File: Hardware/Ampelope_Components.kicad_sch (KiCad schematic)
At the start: 101 parts, among them J18 SWD_Header, J19 USB_B_Micro, Q1 MMBT3904, Q2 MMBT3904, Q3 MMBT3904, Q4 MMBT3904, U1 STM32G431RB, U2 AS3364, U3 LM1117-3.3, U4 TL074, U5 TL074, U6 TL074, Y1 8MHz 20pF

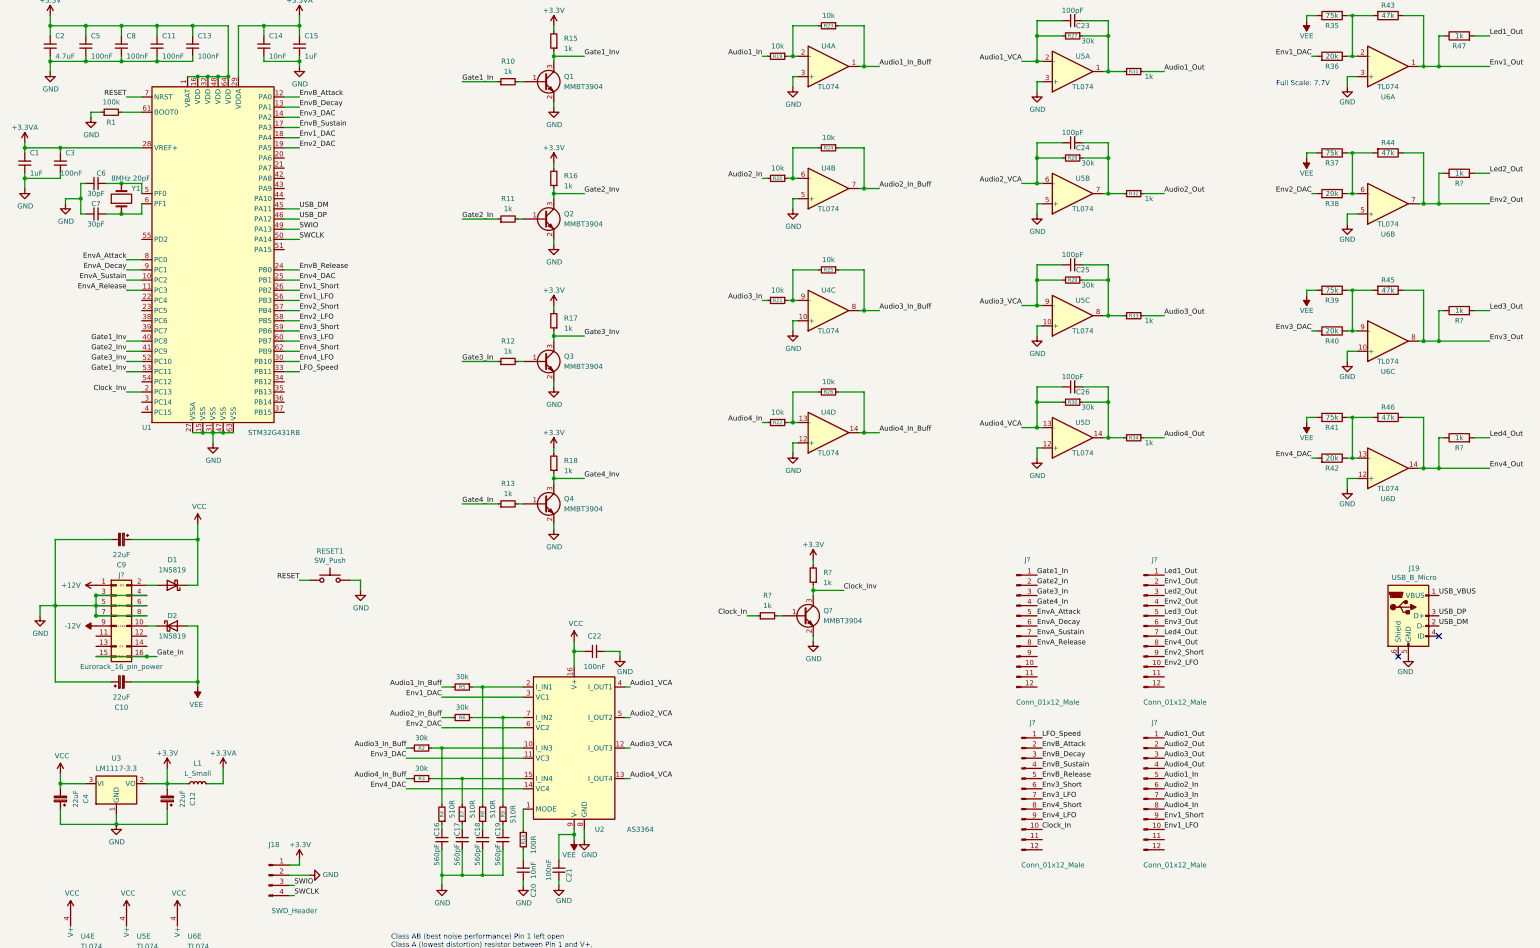
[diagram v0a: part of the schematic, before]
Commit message: Started rough placement of component board
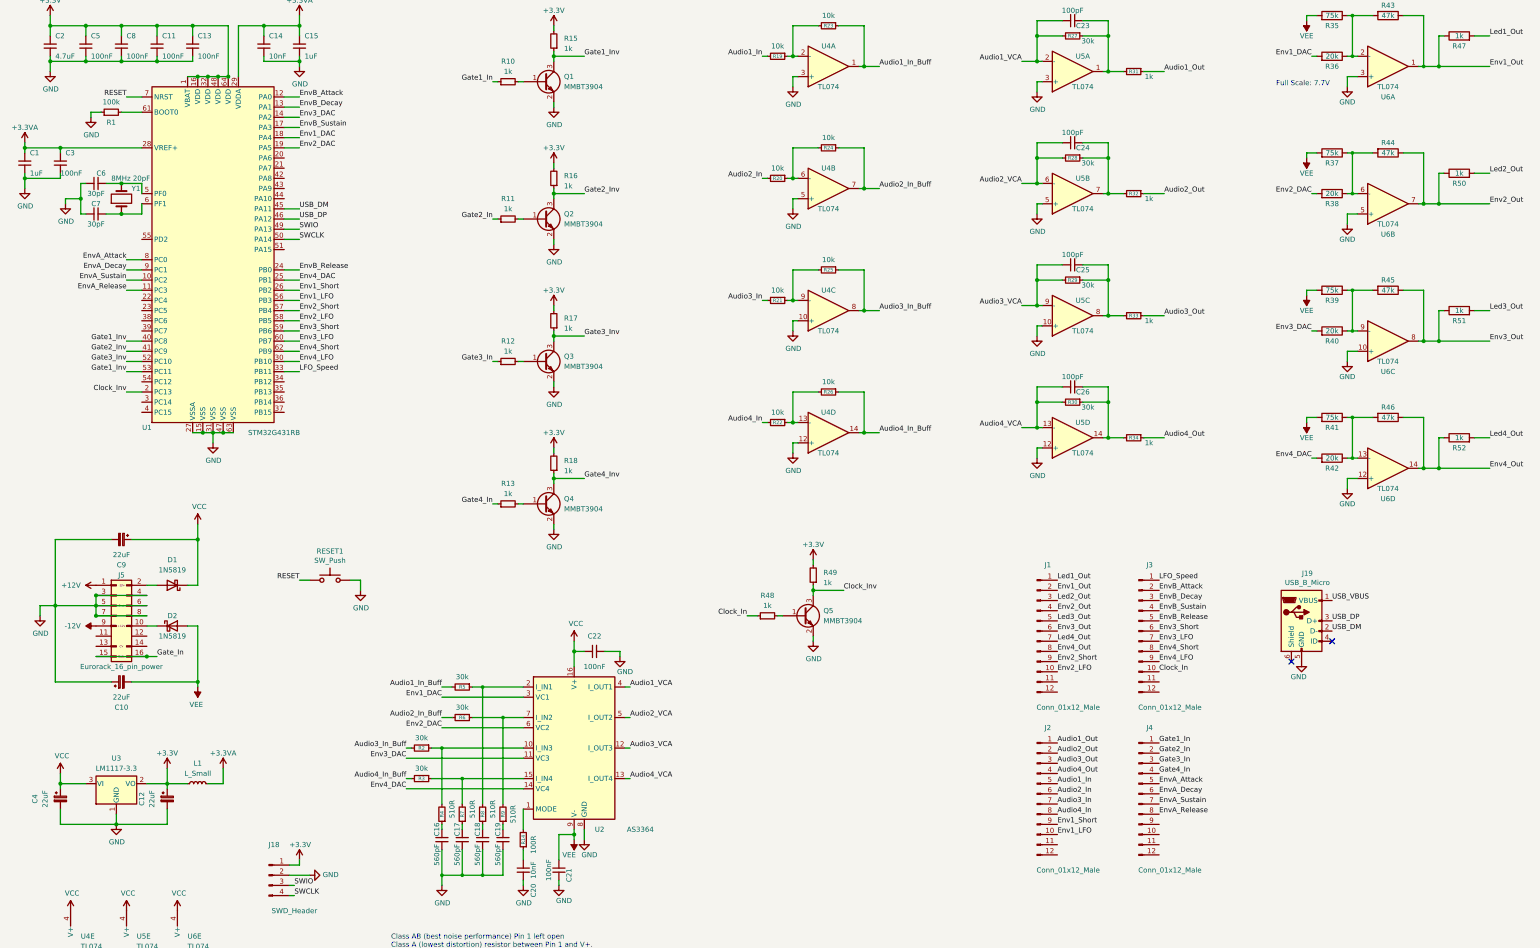
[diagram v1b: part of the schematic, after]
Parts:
- J1, J2, J3, J4: renamed from J?; footprint (none) -> Connector_PinHeader_2.54mm:PinHeader_1x12_P2.54mm_Vertical
- J5: renamed from J?; footprint (none) -> Custom_Footprints:Eurorack_16_pin_header
- gave numbers to parts that had none: 6
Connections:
- net +3V3: now also C12.1; no longer C12.2
- net GND: now also C12.2, C4.2; no longer C12.1, C4.1
- net VCC: now also C4.1; no longer C4.2
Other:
- moved on the sheet: C12, C4, J1, J19, J2, J3, J4

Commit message: More layout of component board
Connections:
- net +12V: now also D1.2 (A), J5.2 (Pin_2)
- net -12V: now also D2.1 (K), J5.10 (Pin_10)
- net Env1_Short: now also U1.42 (PA8); no longer U1.26 (PB2)
- net Env4_LFO: now also U1.43 (PA9); no longer U1.30 (PB10)
- net BOOT0: now reaches R1.2, U1.61 (BOOT0)
- no-connect marks 2 -> 6
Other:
- moved on the sheet: R1
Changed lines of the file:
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@@
   (junction (at 35.56 29.21) (diameter 1.016) (color 0 0 0 0))
   (junction (at 35.56 38.1) (diameter 1.016) (color 0 0 0 0))
+  (junction (at 38.1 168.91) (diameter 1.016) (color 0 0 0 0))
   (junction (at 38.1 171.45) (diameter 1.016) (color 0 0 0 0))
   (junction (at 38.1 173.99) (diameter 1.016) (color 0 0 0 0))
   (junction (at 38.1 176.53) (diameter 1.016) (color 0 0 0 0))
+  (junction (at 38.1 179.07) (diameter 1.016) (color 0 0 0 0))
   (junction (at 43.18 228.6) (diameter 1.016) (color 0 0 0 0))
   (junction (at 44.45 29.21) (diameter 1.016) (color 0 0 0 0))
@@
   (junction (at 44.45 68.58) (diameter 1.016) (color 0 0 0 0))
   (junction (at 44.45 76.2) (diameter 1.016) (color 0 0 0 0))
+  (junction (at 50.8 168.91) (diameter 1.016) (color 0 0 0 0))
+  (junction (at 50.8 179.07) (diameter 1.016) (color 0 0 0 0))
   (junction (at 50.8 186.69) (diameter 1.016) (color 0 0 0 0))
   (junction (at 53.34 29.21) (diameter 1.016) (color 0 0 0 0))
@@
   (junction (at 373.38 107.95) (diameter 1.016) (color 0 0 0 0))
   (junction (at 373.38 139.7) (diameter 1.016) (color 0 0 0 0))
+  (no_connect (at 38.1 181.61))
+  (no_connect (at 38.1 184.15))
+  (no_connect (at 50.8 181.61))
+  (no_connect (at 50.8 184.15))
   (no_connect (at 336.55 187.96))
   (no_connect (at 346.71 182.88))
@@
     (stroke (width 0) (type solid) (color 0 0 0 0))
   )
+  (wire (pts (xy 30.48 50.8) (xy 33.02 50.8))
+    (stroke (width 0) (type solid) (color 0 0 0 0))
+  )
+  (wire (pts (xy 30.48 52.07) (xy 30.48 50.8))
+    (stroke (width 0) (type solid) (color 0 0 0 0))
+  )
   (wire (pts (xy 30.48 72.39) (xy 34.29 72.39))
     (stroke (width 0) (type solid) (color 0 0 0 0))
@@
     (stroke (width 0) (type solid) (color 0 0 0 0))
   )
-  (wire (pts (xy 36.83 50.8) (xy 39.37 50.8))
-    (stroke (width 0) (type solid) (color 0 0 0 0))
-  )
-  (wire (pts (xy 36.83 52.07) (xy 36.83 50.8))
+  (wire (pts (xy 38.1 50.8) (xy 49.53 50.8))
+    (stroke (width 0) (type solid) (color 0 0 0 0))
+  )
+  (wire (pts (xy 38.1 168.91) (xy 50.8 168.91))
     (stroke (width 0) (type solid) (color 0 0 0 0))
   )
@@
     (stroke (width 0) (type solid) (color 0 0 0 0))
   )
+  (wire (pts (xy 38.1 179.07) (xy 50.8 179.07))
+    (stroke (width 0) (type solid) (color 0 0 0 0))
+  )
   (wire (pts (xy 38.1 186.69) (xy 50.8 186.69))
     (stroke (width 0) (type solid) (color 0 0 0 0))
@@
     (stroke (width 0) (type solid) (color 0 0 0 0))
   )
-  (wire (pts (xy 44.45 50.8) (xy 49.53 50.8))
-    (stroke (width 0) (type solid) (color 0 0 0 0))
-  )
   (wire (pts (xy 44.45 68.58) (xy 49.53 68.58))
     (stroke (width 0) (type solid) (color 0 0 0 0))
@@
     (stroke (width 0) (type solid) (color 0 0 0 0))
   )
+  (wire (pts (xy 85.09 67.31) (xy 88.9 67.31))
+    (stroke (width 0) (type solid) (color 0 0 0 0))
+  )
+  (wire (pts (xy 85.09 69.85) (xy 88.9 69.85))
+    (stroke (width 0) (type solid) (color 0 0 0 0))
+  )
   (wire (pts (xy 85.09 74.93) (xy 88.9 74.93))
     (stroke (width 0) (type solid) (color 0 0 0 0))
@@
     (stroke (width 0) (type solid) (color 0 0 0 0))
   )
-  (wire (pts (xy 85.09 95.25) (xy 88.9 95.25))
-    (stroke (width 0) (type solid) (color 0 0 0 0))
-  )
   (wire (pts (xy 85.09 97.79) (xy 88.9 97.79))
     (stroke (width 0) (type solid) (color 0 0 0 0))
@@
   )
   (wire (pts (xy 85.09 110.49) (xy 88.9 110.49))
-    (stroke (width 0) (type solid) (color 0 0 0 0))
-  )
-  (wire (pts (xy 85.09 113.03) (xy 88.9 113.03))
     (stroke (width 0) (type solid) (color 0 0 0 0))
   )
@@
     (effects (font (size 1.27 1.27)) (justify left bottom))
   )
+  (label "BOOT0" (at 39.37 50.8 0)
+    (effects (font (size 1.27 1.27)) (justify left bottom))
+  )
   (label "RESET" (at 45.72 46.99 180)
     (effects (font (size 1.27 1.27)) (justify right bottom))
@@
     (effects (font (size 1.27 1.27)) (justify left bottom))
   )
+  (label "Env1_Short" (at 88.9 67.31 0)
+    (effects (font (size 1.27 1.27)) (justify left bottom))
+  )
+  (label "Env4_LFO" (at 88.9 69.85 0)
+    (effects (font (size 1.27 1.27)) (justify left bottom))
+  )
   (label "USB_DM" (at 88.9 74.93 0)
     (effects (font (size 1.27 1.27)) (justify left bottom))
@@
     (effects (font (size 1.27 1.27)) (justify left bottom))
   )
-  (label "Env1_Short" (at 88.9 95.25 0)
-    (effects (font (size 1.27 1.27)) (justify left bottom))
-  )
   (label "Env1_LFO" (at 88.9 97.79 0)
     (effects (font (size 1.27 1.27)) (justify left bottom))
@@
   )
   (label "Env4_Short" (at 88.9 110.49 0)
-    (effects (font (size 1.27 1.27)) (justify left bottom))
-  )
-  (label "Env4_LFO" (at 88.9 113.03 0)
     (effects (font (size 1.27 1.27)) (justify left bottom))
   )
@@
     (pin "1")
   )
+  (symbol (lib_id "power:GND") (at 30.48 52.07 0) (unit 1)
+    (in_bom yes) (on_board yes)
+    (property "Reference" "#PWR010" (id 0) (at 30.48 58.42 0)
+      (effects (font (size 1.27 1.27)) hide)
+    )
+    (property "Value" "GND" (id 1) (at 30.607 56.4642 0))
+    (property "Footprint" "" (id 2) (at 30.48 52.07 0)
+      (effects (font (size 1.27 1.27)) hide)
+    )
+    (property "Datasheet" "" (id 3) (at 30.48 52.07 0)
+      (effects (font (size 1.27 1.27)) hide)
+    )
+    (pin "1")
+  )
   (symbol (lib_id "power:GND") (at 30.48 73.66 0) (unit 1)
     (in_bom yes) (on_board yes)
@@
     (pin "1")
   )
-  (symbol (lib_id "power:GND") (at 36.83 52.07 0) (unit 1)
-    (in_bom yes) (on_board yes)
-    (property "Reference" "#PWR010" (id 0) (at 36.83 58.42 0)
-      (effects (font (size 1.27 1.27)) hide)
-    )
-    (property "Value" "GND" (id 1) (at 36.957 56.4642 0))
-    (property "Footprint" "" (id 2) (at 36.83 52.07 0)
-      (effects (font (size 1.27 1.27)) hide)
-    )
-    (property "Datasheet" "" (id 3) (at 36.83 52.07 0)
-      (effects (font (size 1.27 1.27)) hide)
-    )
-    (pin "1")
-  )
   (symbol (lib_id "power:GND") (at 43.18 228.6 0) (unit 1)
     (in_bom yes) (on_board yes)
@@
     (pin "1")
   )
-  (symbol (lib_id "Device:R_Small") (at 41.91 50.8 90) (unit 1)
-    (in_bom yes) (on_board yes)
-    (property "Reference" "R1" (id 0) (at 41.91 53.34 90))
-    (property "Value" "100k" (id 1) (at 41.91 48.26 90))
-    (property "Footprint" "Resistor_SMD:R_0603_1608Metric_Pad0.98x0.95mm_HandSolder" (id 2) (at 41.91 50.8 0)
-      (effects (font (size 1.27 1.27)) hide)
-    )
-    (property "Datasheet" "~" (id 3) (at 41.91 50.8 0)
-      (effects (font (size 1.27 1.27)) hide)
-    )
+  (symbol (lib_id "Device:R_Small") (at 35.56 50.8 90) (unit 1)
+    (in_bom yes) (on_board yes)
+    (property "Reference" "R1" (id 0) (at 35.56 53.34 90))
+    (property "Value" "100k" (id 1) (at 35.56 48.26 90))
+    (property "Footprint" "Resistor_SMD:R_0603_1608Metric_Pad0.98x0.95mm_HandSolder" (id 2) (at 35.56 50.8 0)
+      (effects (font (size 1.27 1.27)) hide)
+    )
+    (property "Datasheet" "~" (id 3) (at 35.56 50.8 0)
+      (effects (font (size 1.27 1.27)) hide)
+    )
